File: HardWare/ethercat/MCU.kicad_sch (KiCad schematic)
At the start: 40 parts, among them J2 Conn_01x03, J3 Conn_01x04, J6 Conn_01x03, J7 Conn_01x04, SW1 SW_Push, U5 STM32F407VETx, U6 TJA1051T-3, U7 TJA1051T-3, Y1 8M, Y2 32.768KHz

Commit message: Add test version
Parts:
- added C57, C58, C59, C60, C61, C62, C63, C64, C65: 100n, Capacitor_SMD:C_0603_1608Metric, symbol Device:C
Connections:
- net VCC is gone; now on net 3V3: U6.5 (VIO), U7.5 (VIO)
- net 3V3: now also C57.1, C58.1, C59.1, C60.1, C61.1, C62.1, C63.1, C64.1, C65.1
- net GND: now also C57.2, C58.2, C59.2, C60.2, C61.2, C62.2, C63.2, C64.2, C65.2
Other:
- moved on the sheet: R27, U7

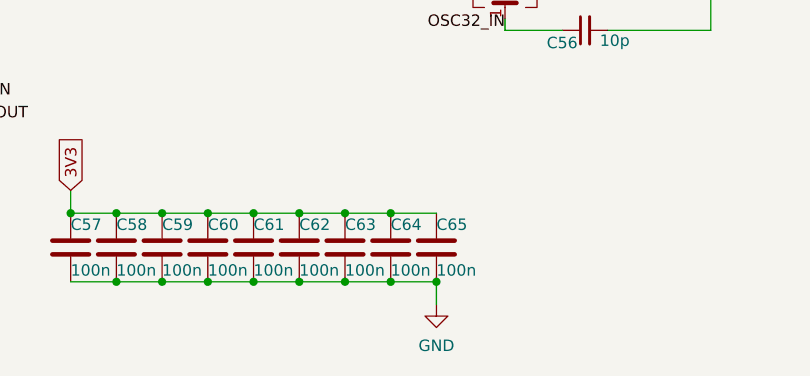
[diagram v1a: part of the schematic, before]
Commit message: 'ethercat_shield' PCB_layout completed
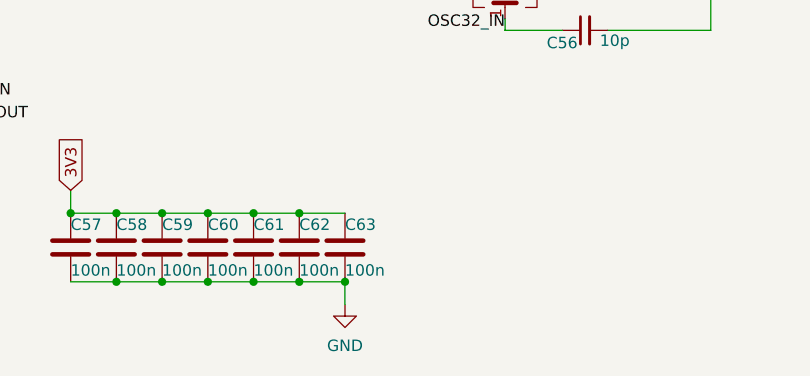
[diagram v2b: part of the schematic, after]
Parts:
- removed C64, C65: 100n, Capacitor_SMD:C_0603_1608Metric, symbol Device:C
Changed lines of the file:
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@@
   (junction (at 259.08 132.08) (diameter 0) (color 0 0 0 0)
   )
-  (junction (at 161.29 185.42) (diameter 0) (color 0 0 0 0)
-  )
   (junction (at 199.39 64.77) (diameter 0) (color 0 0 0 0)
   )
@@
   (junction (at 259.08 101.6) (diameter 0) (color 0 0 0 0)
   )
-  (junction (at 166.37 185.42) (diameter 0) (color 0 0 0 0)
-  )
   (junction (at 259.08 96.52) (diameter 0) (color 0 0 0 0)
   )
@@
   (junction (at 140.97 185.42) (diameter 0) (color 0 0 0 0)
   )
-  (junction (at 156.21 177.8) (diameter 0) (color 0 0 0 0)
-  )
   (junction (at 151.13 177.8) (diameter 0) (color 0 0 0 0)
   )
@@
   )
   (junction (at 135.89 185.42) (diameter 0) (color 0 0 0 0)
-  )
-  (junction (at 161.29 177.8) (diameter 0) (color 0 0 0 0)
   )
   (no_connect (at 110.49 88.9))
@@
     (stroke (width 0) (type default) (color 0 0 0 0))
   )
-  (wire (pts (xy 161.29 177.8) (xy 166.37 177.8))
-    (stroke (width 0) (type default) (color 0 0 0 0))
-  )
   (wire (pts (xy 130.81 185.42) (xy 135.89 185.42))
     (stroke (width 0) (type default) (color 0 0 0 0))
@@
     (stroke (width 0) (type default) (color 0 0 0 0))
   )
-  (wire (pts (xy 166.37 185.42) (xy 166.37 187.96))
-    (stroke (width 0) (type default) (color 0 0 0 0))
-  )
   (wire (pts (xy 186.944 39.116) (xy 192.024 39.116))
     (stroke (width 0) (type default) (color 0 0 0 0))
@@
     (stroke (width 0) (type default) (color 0 0 0 0))
   )
+  (wire (pts (xy 156.21 187.96) (xy 156.21 185.42))
+    (stroke (width 0) (type default) (color 0 0 0 0))
+  )
   (wire (pts (xy 64.77 55.88) (xy 40.64 55.88))
     (stroke (width 0) (type default) (color 0 0 0 0))
@@
     (stroke (width 0) (type default) (color 0 0 0 0))
   )
-  (wire (pts (xy 161.29 185.42) (xy 166.37 185.42))
-    (stroke (width 0) (type default) (color 0 0 0 0))
-  )
   (wire (pts (xy 217.17 65.786) (xy 217.17 69.85))
     (stroke (width 0) (type default) (color 0 0 0 0))
@@
     (stroke (width 0) (type default) (color 0 0 0 0))
   )
-  (wire (pts (xy 156.21 177.8) (xy 161.29 177.8))
-    (stroke (width 0) (type default) (color 0 0 0 0))
-  )
   (wire (pts (xy 214.122 144.78) (xy 214.122 147.066))
-    (stroke (width 0) (type default) (color 0 0 0 0))
-  )
-  (wire (pts (xy 156.21 185.42) (xy 161.29 185.42))
     (stroke (width 0) (type default) (color 0 0 0 0))
   )
@@
     (pin "2")
   )
-  (symbol (lib_id "Device:C") (at 166.37 181.61 0) (unit 1)
-    (in_bom yes) (on_board yes)
-    (property "Reference" "C65" (id 0) (at 166.37 179.07 0)
-      (effects (font (size 1.27 1.27)) (justify left))
-    )
-    (property "Value" "100n" (id 1) (at 166.37 184.15 0)
-      (effects (font (size 1.27 1.27)) (justify left))
-    )
-    (property "Footprint" "Capacitor_SMD:C_0603_1608Metric" (id 2) (at 167.3352 185.42 0)
-      (effects (font (size 1.27 1.27)) hide)
-    )
-    (property "Datasheet" "~" (id 3) (at 166.37 181.61 0)
-      (effects (font (size 1.27 1.27)) hide)
-    )
-    (pin "1")
-    (pin "2")
-  )
   (symbol (lib_id "Device:R_Small") (at 250.19 53.848 180) (unit 1)
     (in_bom yes) (on_board yes)
@@
     )
     (pin "1")
-  )
-  (symbol (lib_id "Device:C") (at 161.29 181.61 0) (unit 1)
-    (in_bom yes) (on_board yes)
-    (property "Reference" "C64" (id 0) (at 161.29 179.07 0)
-      (effects (font (size 1.27 1.27)) (justify left))
-    )
-    (property "Value" "100n" (id 1) (at 161.29 184.15 0)
-      (effects (font (size 1.27 1.27)) (justify left))
-    )
-    (property "Footprint" "Capacitor_SMD:C_0603_1608Metric" (id 2) (at 162.2552 185.42 0)
-      (effects (font (size 1.27 1.27)) hide)
-    )
-    (property "Datasheet" "~" (id 3) (at 161.29 181.61 0)
-      (effects (font (size 1.27 1.27)) hide)
-    )
-    (pin "1")
-    (pin "2")
   )
   (symbol (lib_id "Device:C") (at 125.73 181.61 0) (unit 1)
@@
     (pin "1")
   )
+  (symbol (lib_id "power:GND") (at 156.21 187.96 0) (unit 1)
+    (in_bom yes) (on_board yes)
+    (property "Reference" "#PWR?" (id 0) (at 156.21 194.31 0)
+      (effects (font (size 1.27 1.27)) hide)
+    )
+    (property "Value" "GND" (id 1) (at 156.21 192.5225 0))
+    (property "Footprint" "" (id 2) (at 156.21 187.96 0)
+      (effects (font (size 1.27 1.27)) hide)
+    )
+    (property "Datasheet" "" (id 3) (at 156.21 187.96 0)
+      (effects (font (size 1.27 1.27)) hide)
+    )
+    (pin "1")
+  )
   (symbol (lib_id "power:GND") (at 167.64 152.4 270) (unit 1)
     (in_bom yes) (on_board yes) (fields_autoplaced)
@@
       (effects (font (size 1.27 1.27)) hide)
     )
-    (pin "1")
-  )
-  (symbol (lib_id "power:GND") (at 166.37 187.96 0) (unit 1)
-    (in_bom yes) (on_board yes)
-    (property "Reference" "#PWR0144" (id 0) (at 166.37 194.31 0)
-      (effects (font (size 1.27 1.27)) hide)
-    )
-    (property "Value" "GND" (id 1) (at 166.37 192.5225 0))
-    (property "Footprint" "" (id 2) (at 166.37 187.96 0)
-      (effects (font (size 1.27 1.27)) hide)
-    )
-    (property "Datasheet" "" (id 3) (at 166.37 187.96 0)
-      (effects (font (size 1.27 1.27)) hide)
-    )

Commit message: Official version-EtherCAT2CAN_NUC
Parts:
- removed C50, C51: 2.2u, Capacitor_SMD:C_0603_1608Metric, symbol Device:C
- removed C52, C54: 10u, Capacitor_SMD:C_0603_1608Metric, symbol Device:C
- removed C53, C59, C61: 100n, Capacitor_SMD:C_0603_1608Metric, symbol Device:C
- removed C55, C56: 10p, Capacitor_SMD:C_0603_1608Metric, symbol Device:C_Small
- removed D6: GREEN, LED_SMD:LED_0603_1608Metric, symbol Device:LED
- removed J2, J6: Conn_01x03, Connector_JST:JST_GH_SM03B-GHS-TB_1x03-1MP_P1.25mm_Horizontal, symbol Connector_Generic:Conn_01x03
- removed J3, J7: Conn_01x04, Connector_JST:JST_GH_SM04B-GHS-TB_1x04-1MP_P1.25mm_Horizontal, symbol Connector_Generic:Conn_01x04
- removed R25: 1K, Resistor_SMD:R_0603_1608Metric, symbol Device:R_Small
- removed R44, R48: 10K, Resistor_SMD:R_0603_1608Metric, symbol Device:R_Small
- removed R45: 10, Resistor_SMD:R_0603_1608Metric, symbol Device:R_Small
- removed R46, R47: 0, Resistor_SMD:R_0603_1608Metric, symbol Device:R_Small
- removed R49: 10K, Resistor_SMD:R_0603_1608Metric, symbol Device:R
- removed R50: 1M, Resistor_SMD:R_0603_1608Metric, symbol Device:R_Small
- removed SW1: SW_Push, Button_Switch_SMD:SW_SPST_FSMSM, symbol Switch:SW_Push
- removed U5: STM32F407VETx, Package_QFP:LQFP-100_14x14mm_P0.5mm, symbol MCU_ST_STM32F4:STM32F407VETx
- removed Y2: 32.768KHz, Crystal:Crystal_SMD_3225-4Pin_3.2x2.5mm, symbol Device:Crystal_GND24
- added C1, C64: 100n, Capacitor_SMD:C_0402_1005Metric, symbol Device:C
- added C2: 4.7u, Capacitor_SMD:C_0402_1005Metric, symbol Device:C
- added J6: Conn_01x06, Connector_JST:JST_GH_SM06B-GHS-TB_1x06-1MP_P1.25mm_Horizontal, symbol Connector_Generic:Conn_01x06
- added R1: 10K, Resistor_SMD:R_0402_1005Metric, symbol Device:R_Small
- added U1: ~, Package_TO_SOT_SMD:SOT-23-5, symbol Extra IC:ESDS314
- added U10: STM32F412RETx, Package_QFP:LQFP-64_10x10mm_P0.5mm, symbol MCU_ST_STM32F4:STM32F412RETx
- added U11, U5: ~, Package_TO_SOT_SMD:SOT-23-3, symbol Extra IC:PESD1CAN
- C27, C28, C29, C30, C31, C32, C57, C58, C60, C62, C63: footprint Capacitor_SMD:C_0603_1608Metric -> Capacitor_SMD:C_0402_1005Metric
- D3, D4: footprint LED_SMD:LED_0603_1608Metric -> LED_SMD:LED_0402_1005Metric
- D5: value GREEN -> BLUE; footprint LED_SMD:LED_0603_1608Metric -> LED_SMD:LED_0402_1005Metric
- R22, R23, R24, R26, R27: footprint Resistor_SMD:R_0603_1608Metric -> Resistor_SMD:R_0402_1005Metric
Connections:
- net +5V: now also J6.6 (Pin_6)
- net 3V3: now also C64.1, U10.1 (VBAT), U10.13 (VDDA), U10.19 (VDD), U10.32 (VDD), U10.48 (VDD), U10.64 (VDD)
- net CAN0_H: now also U5.1 (H)
- net CAN0_L: now also U5.2 (L)
- net CAN0_RX: now also U10.44 (PA11)
- net CAN0_TX: now also U10.45 (PA12)
- net CAN1_H: now also U11.1 (H)
- net CAN1_L: now also U11.2 (L)
- net CAN1_RX: now also U10.33 (PB12)
- net CAN1_TX: now also U10.34 (PB13)
- net ESC_INT: now also U10.26 (PB0)
- net ESC_MISO: now also U10.22 (PA6)
- net ESC_MOSI: now also U10.23 (PA7)
- net ESC_RSTN: now also U10.36 (PB15)
- net ESC_SCK: now also U10.21 (PA5)
- net ESC_SCS: now also U10.20 (PA4)
- net ESC_SYNC: now also U10.9 (PC1)
- net GND: now also C1.1, C2.1, C64.2, J6.1 (Pin_1), R1.1, U1.2 (GND), U10.12 (VSSA), U10.18 (VSS), U10.31 (VSS), U10.47 (VSS), U10.63 (VSS), U11.3 (GND), U5.3 (GND)
- net OSC_IN: now also U10.5 (PH0)
- net OSC_OUT: now also U10.6 (PH1)
- net SWCLK: now also J6.3 (Pin_3), U10.49 (PA14)
- net SWDIO: now also J6.2 (Pin_2), U10.46 (PA13)
- net LED1 renamed LED_CAN1
- net LED_CAN1: now also U10.35 (PB14)
- net LED2 renamed LED_CAN0
- net LED_CAN0: now also U10.51 (PC10)
- net LED3 renamed LED_UART
- net LED_UART: now also U10.50 (PA15)
- new net: C2.2, U10.30 (VCAP_1)
- new net: R1.2, U10.60 (BOOT0)
- new net: C1.2, U10.7 (NRST)
- new net USART_RX: J6.5 (Pin_5), U1.4 (I/O1), U10.43 (PA10)
- new net USART_TX: J6.4 (Pin_4), U1.5 (I/O2), U10.42 (PA9)
- no-connect marks 52 -> 32
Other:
- moved on the sheet: C27, C28, D3, D4, D5, R22, R23, R24, Y1
